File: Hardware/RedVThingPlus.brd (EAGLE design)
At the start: 58.4 x 22.9 mm, 139 parts, among them J1 FEMALE 2x3, J2 USB Female Type C Connector, J4 QWIIC_RIGHT_ANGLE, Q1 3.1A/30V/105mΩ, U1 MCP73831, U2 AP2127K-1.8V, U3 AP2112-3.3V, U4 MK22FN128VLH10, U5 32MBit, U6 FE310, Y1 32.768KHZ, Y2 16MHz

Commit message: post qc double check changes
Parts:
- removed LED2: RED, SparkFun-LED:LED-1206
- removed R2: 10k, SparkFun-Resistors:0603
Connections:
- removed net N$2: LED2.A, R2.1
- net 5V: no longer R2.2
- net GND: no longer LED2.C
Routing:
- net 5V: track 21.8 -> 19.2 mm
- net N$2: track 2.37 -> 0.00 mm
- net RXI: track 21.4 -> 19.9 mm
- net SPI_SCK: track 16.3 -> 17.4 mm
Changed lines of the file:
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@@
 <layer number="23" name="tOrigins" color="15" fill="1" visible="yes" active="yes"/>
 <layer number="24" name="bOrigins" color="15" fill="1" visible="yes" active="yes"/>
-<layer number="25" name="tNames" color="7" fill="1" visible="no" active="yes"/>
+<layer number="25" name="tNames" color="7" fill="1" visible="yes" active="yes"/>
 <layer number="26" name="bNames" color="7" fill="1" visible="no" active="yes"/>
-<layer number="27" name="tValues" color="7" fill="1" visible="no" active="yes"/>
+<layer number="27" name="tValues" color="7" fill="1" visible="yes" active="yes"/>
 <layer number="28" name="bValues" color="7" fill="1" visible="no" active="yes"/>
 <layer number="29" name="tStop" color="2" fill="3" visible="yes" active="yes"/>
@@
 <attribute name="VALUE" x="41.91" y="3.683" size="0.6096" layer="27" font="vector" ratio="20" align="top-center"/>
 </element>
-<element name="R2" library="SparkFun-Resistors" package="0603" value="10k" x="23.542" y="11.176" smashed="yes" rot="R180">
-<attribute name="NAME" x="23.542" y="10.414" size="0.6096" layer="25" font="vector" ratio="20" rot="R180" align="bottom-center"/>
-<attribute name="PROD_ID" value="RES-00824" x="23.542" y="11.176" size="1.778" layer="27" rot="R180" display="off"/>
-<attribute name="VALUE" x="23.542" y="11.938" size="0.6096" layer="27" font="vector" ratio="20" rot="R180" align="top-center"/>
-</element>
 <element name="C10" library="SparkFun-Capacitors" package="0603" value="0.1uF" x="13.208" y="14.478" smashed="yes">
 <attribute name="NAME" x="13.208" y="15.24" size="0.6096" layer="25" font="vector" ratio="20" align="bottom-center"/>
@@
 <attribute name="VALUE" x="10.16" y="6.477" size="0.6096" layer="27" font="vector" ratio="20" align="top-center"/>
 </element>
-<element name="LED2" library="SparkFun-LED" package="LED-1206" value="RED" x="26.67" y="12.446" smashed="yes" rot="R90">
-<attribute name="NAME" x="25.7175" y="12.446" size="0.6096" layer="25" font="vector" ratio="20" rot="R90" align="bottom-center"/>
-<attribute name="PROD_ID" value="DIO-09912" x="26.67" y="12.446" size="1.778" layer="27" rot="R90" display="off"/>
-<attribute name="VALUE" value="RED" x="27.6225" y="12.446" size="0.6096" layer="27" font="vector" ratio="20" rot="R90" align="top-center"/>
-</element>
 <element name="LED1" library="SparkFun-LED" package="LED-0603" value="BLUE" x="41.91" y="3.048" smashed="yes" rot="R180">
 <attribute name="NAME" x="41.91" y="2.0955" size="0.6096" layer="25" font="vector" ratio="20" rot="R180" align="bottom-center"/>
@@
 </element>
 <element name="R19" library="SparkFun-Resistors" package="0603" value="5.1k" x="9.525" y="12.7" smashed="yes" rot="R180">
-<attribute name="NAME" x="81.915" y="-12.192" size="0.6096" layer="25" font="vector" ratio="20" rot="R180" align="bottom-center"/>
+<attribute name="NAME" x="9.5035" y="12.0635" size="0.6096" layer="25" font="vector" ratio="20" rot="R180" align="bottom-center"/>
 <attribute name="PROD_ID" value="RES-12083" x="9.525" y="12.7" size="1.778" layer="27" rot="R180" display="off"/>
 <attribute name="VALUE" x="9.525" y="13.462" size="0.6096" layer="27" font="vector" ratio="20" rot="R180" align="top-center"/>
@@
 <signal name="5V">
 <contactref element="U2" pad="1"/>
-<contactref element="R2" pad="2"/>
 <contactref element="U3" pad="1"/>
 <contactref element="R4" pad="1"/>
@@
 <wire x1="23.495" y1="3.644" x2="23.495" y2="6.477" width="0.2032" layer="1"/>
 <wire x1="23.495" y1="6.477" x2="23.18" y2="6.792" width="0.2032" layer="1"/>
-<wire x1="21.717" y1="11.176" x2="22.692" y2="11.176" width="0.2032" layer="1"/>
 <wire x1="21.209" y1="6.792" x2="21.209" y2="9.779" width="0.2032" layer="1"/>
-<wire x1="21.209" y1="9.779" x2="21.209" y2="10.668" width="0.2032" layer="1"/>
-<wire x1="21.209" y1="10.668" x2="21.717" y2="11.176" width="0.2032" layer="1"/>
 <wire x1="22.1949" y1="9.84" x2="21.27" y2="9.84" width="0.2032" layer="1"/>
 <wire x1="21.27" y1="9.84" x2="21.209" y2="9.779" width="0.2032" layer="1"/>
 </signal>
 <signal name="GND">
-<contactref element="LED2" pad="C"/>
 <contactref element="LED1" pad="C"/>
 <contactref element="C16" pad="2"/>
@@
 <wire x1="57.277" y1="13.97" x2="57.277" y2="15.748" width="0.2032" layer="16"/>
 </signal>
-<signal name="N$2">
-<contactref element="R2" pad="1"/>
-<contactref element="LED2" pad="A"/>
-<wire x1="26.67" y1="10.946" x2="25.63" y2="10.946" width="0.2032" layer="1"/>
-<wire x1="25.4" y1="11.176" x2="24.392" y2="11.176" width="0.2032" layer="1"/>
-<wire x1="25.63" y1="10.946" x2="25.4" y2="11.176" width="0.2032" layer="1"/>
-</signal>
 <signal name="VUSB">
 <contactref element="F1" pad="1"/>
@@
 <wire x1="46.99" y1="18.5843" x2="46.6937" y2="18.288" width="0.1524" layer="16"/>
 <wire x1="46.99" y1="16.8002" x2="47.355" y2="16.4352" width="0.1524" layer="1"/>
-<wire x1="46.99" y1="17.5542" x2="46.99" y2="17.5542" width="0.1524" layer="1"/>
 <wire x1="46.99" y1="16.8002" x2="46.99" y2="18.5843" width="0.1524" layer="1"/>
 <via x="46.99" y="18.5843" extent="1-16" drill="0.35"/>
@@
 <contactref element="J7" pad="3"/>
 <wire x1="40.95055" y1="9.271" x2="40.7242" y2="9.49735" width="0.1524" layer="1"/>
-<wire x1="44.45" y1="9.271" x2="44.555" y2="9.376" width="0.1524" layer="1"/>
 <wire x1="42.545" y1="9.271" x2="44.45" y2="9.271" width="0.1524" layer="1"/>
 <wire x1="49.53" y1="1.27" x2="48.514" y2="2.286" width="0.2032" layer="1"/>
-<via x="42.7002" y="3.556" extent="1-16" drill="0.35"/>
-<wire x1="42.672" y1="7.84576875" x2="42.813115625" y2="7.986884375" width="0.1524" layer="16"/>
-<wire x1="42.813115625" y1="7.986884375" x2="43.130615625" y2="8.304384375" width="0.1524" layer="16"/>
+<via x="43.8327" y="3.112" extent="1-16" drill="0.35"/>
 <wire x1="43.130615625" y1="8.304384375" x2="43.130615625" y2="8.763" width="0.1524" layer="16"/>
 <via x="42.545" y="9.271" extent="1-16" drill="0.35"/>
@@
 <wire x1="43.130615625" y1="8.763" x2="42.622615625" y2="9.271" width="0.1524" layer="16"/>
 <wire x1="42.622615625" y1="9.271" x2="42.545" y2="9.271" width="0.1524" layer="16"/>
-<wire x1="42.813115625" y1="7.986884375" x2="42.672" y2="7.84576875" width="0.1524" layer="16"/>
-<wire x1="42.672" y1="7.84576875" x2="42.3192" y2="7.49296875" width="0.1524" layer="16"/>
+<wire x1="43.130615625" y1="8.304384375" x2="42.3192" y2="7.49296875" width="0.1524" layer="16"/>
 <wire x1="42.3192" y1="7.49296875" x2="42.3192" y2="5.222375" width="0.1524" layer="16"/>
 <contactref element="U6" pad="38"/>
@@
 <wire x1="44.555" y1="9.376" x2="44.555" y2="9.775" width="0.1524" layer="1"/>
 <wire x1="40.7242" y1="9.49735" x2="40.7242" y2="10.3298" width="0.1524" layer="1"/>
-<wire x1="40.7242" y1="10.3298" x2="40.509" y2="10.545" width="0.1524" layer="1"/>
 <contactref element="U4" pad="40"/>
 <wire x1="40.7242" y1="10.3298" x2="40.509" y2="10.545" width="0.1524" layer="1"/>
 <wire x1="40.509" y1="10.545" x2="39.99" y2="10.545" width="0.1524" layer="1"/>
-<wire x1="42.7002" y1="4.841375" x2="42.7002" y2="3.556" width="0.1524" layer="16"/>
-<wire x1="42.3192" y1="5.222375" x2="42.7002" y2="4.841375" width="0.1524" layer="16"/>
-<wire x1="48.514" y1="2.286" x2="43.18" y2="2.286" width="0.2032" layer="1"/>
-<wire x1="42.7002" y1="2.7658" x2="42.7002" y2="3.556" width="0.2032" layer="1"/>
-<wire x1="43.18" y1="2.286" x2="42.7002" y2="2.7658" width="0.2032" layer="1"/>
+<wire x1="43.8327" y1="3.708875" x2="43.8327" y2="3.112" width="0.1524" layer="16"/>
+<wire x1="42.3192" y1="5.222375" x2="43.8327" y2="3.708875" width="0.1524" layer="16"/>
+<wire x1="48.514" y1="2.286" x2="45" y2="2.286" width="0.2032" layer="1"/>
+<wire x1="45" y1="2.286" x2="44.8327" y2="2.286" width="0.2032" layer="1"/>
+<wire x1="44.8327" y1="2.286" x2="44.6587" y2="2.286" width="0.2032" layer="1"/>
+<wire x1="44.6587" y1="2.286" x2="43.8327" y2="3.112" width="0.2032" layer="1"/>
 </signal>
 <signal name="TXO">
@@
 <wire x1="42" y1="6.2962" x2="41.41364375" y2="5.70984375" width="0.1524" layer="1"/>
 <wire x1="41.41364375" y1="5.70984375" x2="41.41364375" y2="5.3858" width="0.1524" layer="1"/>
-<wire x1="41.8112" y1="4.98824375" x2="41.06" y2="4.445" width="0" layer="19" extent="1-16"/>
+<wire x1="41.41364375" y1="5.3858" x2="41.06" y2="5.03215625" width="0.1524" layer="1"/>
+<wire x1="41.06" y1="5.03215625" x2="41.06" y2="4.445" width="0.1524" layer="1"/>
 </signal>
 <signal name="IO10">
@@
 <contactref element="I2C" pad="3"/>
 <wire x1="55.372" y1="16.93" x2="55.372" y2="17.526" width="0.2032" layer="1"/>
-<wire x1="57.15" y1="18.5928" x2="57.1274" y2="18.5928" width="0.2032" layer="16"/>
 <wire x1="55.372" y1="17.526" x2="55.626" y2="17.78" width="0.2032" layer="1"/>
 <wire x1="55.9435" y1="17.78" x2="56.1975" y2="18.034" width="0.2032" layer="1"/>

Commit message: updating to final silk
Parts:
- removed LOGO1: SFE_LOGO_NAME_FLAME.1_INCH, SparkFun-Aesthetics:SFE_LOGO_NAME_FLAME_.1
- added U$13: (no value), Red#V_thing_plus_board_silk#02#jpg:RED#V_THING_PLUS_BOARD_SILK#02#JPG
- U$42: device Redfive_logo#04#jpg (3):REDFIVE_LOGO#04#JPG -> Red#V_thing_plus_board_silk#01#jpg:RED#V_THING_PLUS_BOARD_SILK#01#JPG
- U$49: device buzzard_labels (6):THING_PLUS0 -> asdfkjghb#jpg:ASDFKJGHB#JPG
- moved U$49 7.53 mm to (24.9, 11.7)
- moved U$42 0.14 mm to (21.5, 11.5)
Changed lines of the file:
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@@
 <grid distance="1" unitdist="mm" unit="mm" style="lines" multiple="1" display="yes" altdistance="0.0025" altunitdist="inch" altunit="inch"/>
 <layers>
-<layer number="1" name="Top" color="4" fill="1" visible="yes" active="yes"/>
-<layer number="16" name="Bottom" color="1" fill="1" visible="yes" active="yes"/>
-<layer number="17" name="Pads" color="2" fill="1" visible="yes" active="yes"/>
-<layer number="18" name="Vias" color="2" fill="1" visible="yes" active="yes"/>
-<layer number="19" name="Unrouted" color="6" fill="1" visible="yes" active="yes"/>
-<layer number="20" name="Dimension" color="15" fill="1" visible="yes" active="yes"/>
+<layer number="1" name="Top" color="4" fill="1" visible="no" active="yes"/>
+<layer number="16" name="Bottom" color="1" fill="1" visible="no" active="yes"/>
+<layer number="17" name="Pads" color="2" fill="1" visible="no" active="yes"/>
+<layer number="18" name="Vias" color="2" fill="1" visible="no" active="yes"/>
+<layer number="19" name="Unrouted" color="6" fill="1" visible="no" active="yes"/>
+<layer number="20" name="Dimension" color="15" fill="1" visible="no" active="yes"/>
 <layer number="21" name="tPlace" color="16" fill="1" visible="yes" active="yes"/>
 <layer number="22" name="bPlace" color="14" fill="1" visible="yes" active="yes"/>
 <layer number="23" name="tOrigins" color="15" fill="1" visible="yes" active="yes"/>
 <layer number="24" name="bOrigins" color="15" fill="1" visible="yes" active="yes"/>
-<layer number="25" name="tNames" color="7" fill="1" visible="yes" active="yes"/>
+<layer number="25" name="tNames" color="7" fill="1" visible="no" active="yes"/>
 <layer number="26" name="bNames" color="7" fill="1" visible="no" active="yes"/>
-<layer number="27" name="tValues" color="7" fill="1" visible="yes" active="yes"/>
+<layer number="27" name="tValues" color="7" fill="1" visible="no" active="yes"/>
 <layer number="28" name="bValues" color="7" fill="1" visible="no" active="yes"/>
-<layer number="29" name="tStop" color="2" fill="3" visible="yes" active="yes"/>
-<layer number="30" name="bStop" color="5" fill="6" visible="yes" active="yes"/>
-<layer number="31" name="tCream" color="7" fill="4" visible="yes" active="yes"/>
-<layer number="32" name="bCream" color="7" fill="5" visible="yes" active="yes"/>
+<layer number="29" name="tStop" color="2" fill="3" visible="no" active="yes"/>
+<layer number="30" name="bStop" color="5" fill="6" visible="no" active="yes"/>
+<layer number="31" name="tCream" color="7" fill="4" visible="no" active="yes"/>
+<layer number="32" name="bCream" color="7" fill="5" visible="no" active="yes"/>
 <layer number="33" name="tFinish" color="6" fill="3" visible="no" active="yes"/>
 <layer number="34" name="bFinish" color="6" fill="6" visible="no" active="yes"/>
@@
 <layer number="45" name="Holes" color="7" fill="1" visible="no" active="yes"/>
 <layer number="46" name="Milling" color="3" fill="1" visible="no" active="yes"/>
-<layer number="47" name="Measures" color="7" fill="1" visible="yes" active="yes"/>
+<layer number="47" name="Measures" color="7" fill="1" visible="no" active="yes"/>
 <layer number="48" name="Document" color="7" fill="1" visible="no" active="yes"/>
 <layer number="49" name="ReferenceLC" color="13" fill="1" visible="no" active="yes"/>
 <layer number="50" name="ReferenceLS" color="12" fill="1" visible="no" active="yes"/>
-<layer number="51" name="tDocu" color="6" fill="1" visible="yes" active="yes"/>
+<layer number="51" name="tDocu" color="6" fill="1" visible="no" active="yes"/>
 <layer number="52" name="bDocu" color="7" fill="1" visible="no" active="yes"/>
 <layer number="91" name="Nets" color="2" fill="1" visible="no" active="no"/>
@@
 <wire x1="58.42" y1="0" x2="0" y2="0" width="0.2032" layer="20"/>
 <wire x1="0" y1="0" x2="0" y2="22.86" width="0.2032" layer="20"/>
-<dimension x1="0" y1="22.86" x2="58.42" y2="22.86" x3="29.21" y3="29.21" textsize="1.778" layer="20" unit="inch"/>
-<dimension x1="58.42" y1="22.86" x2="58.42" y2="0" x3="63.5" y3="11.43" textsize="1.778" layer="20" unit="inch"/>
+<dimension x1="0" y1="22.86" x2="58.42" y2="22.86" x3="29.21" y3="29.21" textsize="1.778" layer="47" unit="inch"/>
+<dimension x1="58.42" y1="22.86" x2="58.42" y2="0" x3="63.5" y3="11.43" textsize="1.778" layer="47" unit="inch"/>
 </plain>
 <attributes>
@@
 <element name="U$45" library="seggerlogo#png" package="SEGGERLOGO#PNG" value="" x="10.541" y="16.256" rot="MR90"/>
 <element name="U$38" library="buzzard_labels (4)" package="CHG0" value="" x="16.51" y="3.556"/>
-<element name="LOGO1" library="SparkFun-Aesthetics" package="SFE_LOGO_NAME_FLAME_.1" value="SFE_LOGO_NAME_FLAME.1_INCH" x="24.511" y="11.43" rot="MR90"/>
-<element name="U$42" library="Redfive_logo#04#jpg (3)" package="REDFIVE_LOGO#04#JPG" value="" x="21.59" y="11.557" rot="MR90"/>
-<element name="U$49" library="buzzard_labels (6)" package="THING_PLUS0" value="" x="19" y="7" rot="MR90"/>
 <element name="I2C" library="SparkFun-Jumpers" package="SMT-JUMPER_3_NO_NO-SILK" value="JUMPER-SMT_3_NO_NO-SILK" x="57.15" y="17.78" rot="MR90"/>
 <element name="U$50" library="buzzard_labels (8)" package="I2C_______0" value="" x="57.15" y="13.0175" rot="MR90"/>
 <element name="U$46" library="buzzard_labels (9)" package="50" value="" x="38.735" y="3.302"/>
 <element name="LOGO2" library="SparkFun-Aesthetics" package="SFE_LOGO_FLAME_.2" value="SFE_LOGO_FLAME.2_INCH" x="14.859" y="12.1285" rot="R270"/>
+<element name="U$13" library="Red#V_thing_plus_board_silk#02#jpg" package="RED#V_THING_PLUS_BOARD_SILK#02#JPG" value="" x="19.431" y="11.557" rot="MR90"/>
+<element name="U$42" library="Red#V_thing_plus_board_silk#01#jpg" package="RED#V_THING_PLUS_BOARD_SILK#01#JPG" value="" x="21.463" y="11.4935" rot="MR90"/>
+<element name="U$49" library="asdfkjghb#jpg" package="ASDFKJGHB#JPG" value="" x="24.892" y="11.684" rot="MR90"/>
 </elements>
 <signals>

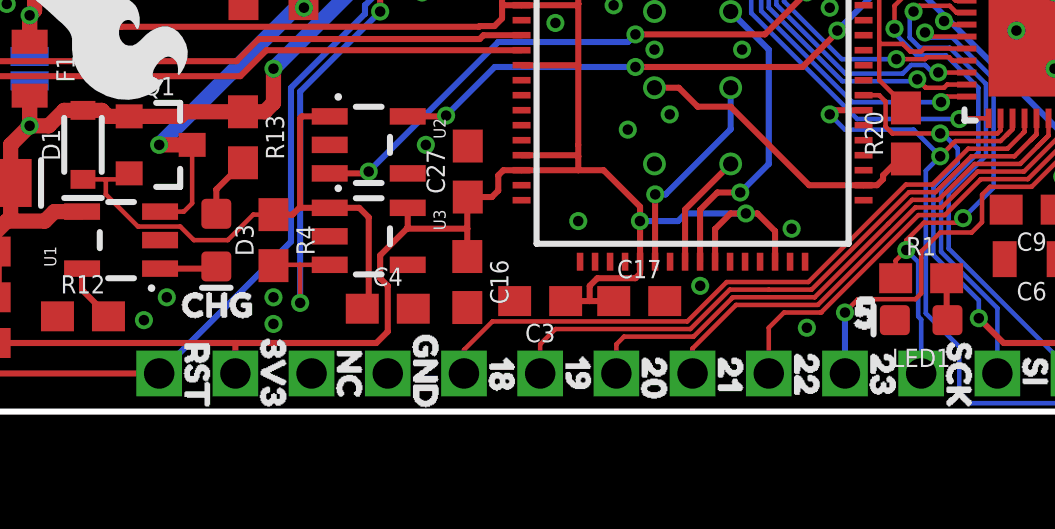
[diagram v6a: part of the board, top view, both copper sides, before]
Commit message: updating silk
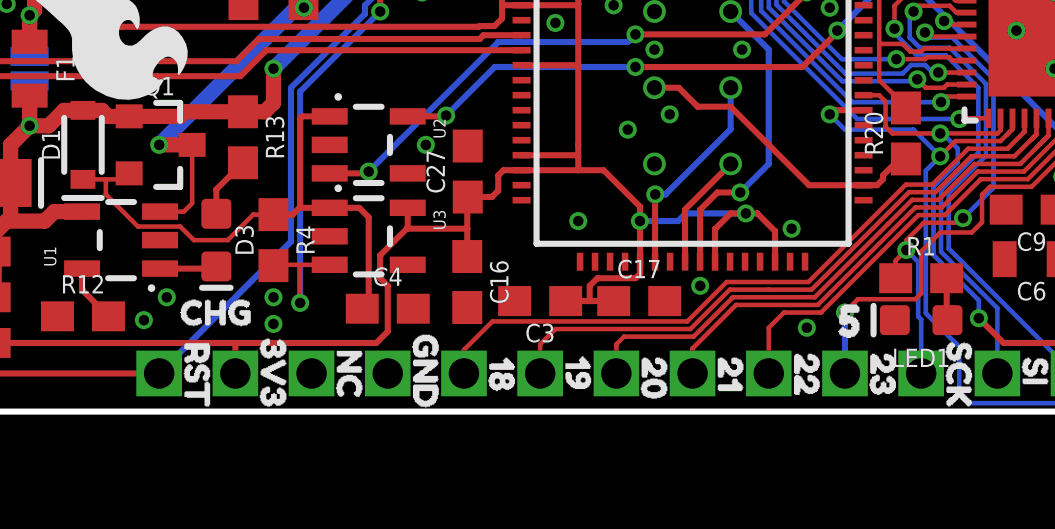
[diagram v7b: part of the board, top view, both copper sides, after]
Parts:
- moved U$46 0.58 mm to (38.2, 3.03)
- moved U$38 0.26 mm to (16.5, 3.30)
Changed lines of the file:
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@@
 <element name="U$69" library="buzzard_labels (3)" package="WAKE0" value="" x="7.112" y="23.495" rot="R270"/>
 <element name="U$45" library="seggerlogo#png" package="SEGGERLOGO#PNG" value="" x="10.541" y="16.256" rot="MR90"/>
-<element name="U$38" library="buzzard_labels (4)" package="CHG0" value="" x="16.51" y="3.556"/>
+<element name="U$38" library="buzzard_labels (4)" package="CHG0" value="" x="16.4645" y="3.3025"/>
 <element name="I2C" library="SparkFun-Jumpers" package="SMT-JUMPER_3_NO_NO-SILK" value="JUMPER-SMT_3_NO_NO-SILK" x="57.15" y="17.78" rot="MR90"/>
 <element name="U$50" library="buzzard_labels (8)" package="I2C_______0" value="" x="57.15" y="13.0175" rot="MR90"/>
-<element name="U$46" library="buzzard_labels (9)" package="50" value="" x="38.735" y="3.302"/>
+<element name="U$46" library="buzzard_labels (9)" package="50" value="" x="38.216" y="3.0325"/>
 <element name="LOGO2" library="SparkFun-Aesthetics" package="SFE_LOGO_FLAME_.2" value="SFE_LOGO_FLAME.2_INCH" x="14.859" y="12.1285" rot="R270"/>
 <element name="U$13" library="Red#V_thing_plus_board_silk#02#jpg" package="RED#V_THING_PLUS_BOARD_SILK#02#JPG" value="" x="19.431" y="11.557" rot="MR90"/>
